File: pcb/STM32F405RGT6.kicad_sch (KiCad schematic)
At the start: 19 parts, among them U1 STM32F405RGTx, Y1 8MHz

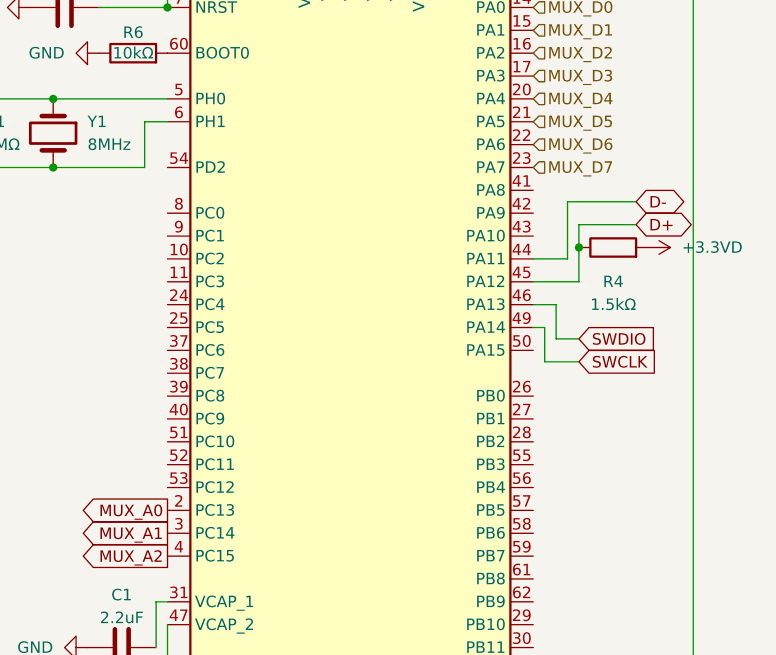
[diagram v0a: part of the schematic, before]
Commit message: feat: added the rotary encoder
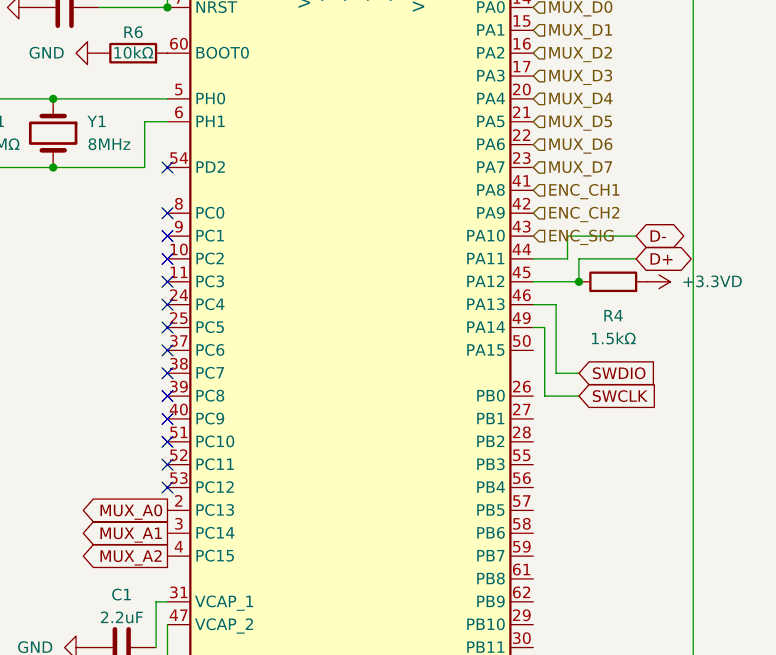
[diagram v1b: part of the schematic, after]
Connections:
- net ENC_CH1: now reaches U1.41 (PA8)
- net ENC_CH2: now reaches U1.42 (PA9)
- net ENC_SIG: now reaches U1.43 (PA10)
- no-connect marks 0 -> 14
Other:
- moved on the sheet: R4
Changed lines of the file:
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@@
+	)
+	(junction
+		(at 121.92 109.22)
+		(diameter 0)
+		(color 0 0 0 0)
 	)
 	(junction
@@
 	)
 	(junction
-		(at 121.92 105.41)
-		(diameter 0)
-		(color 0 0 0 0)
-	)
-	(junction
 		(at 53.34 88.9)
 		(diameter 0)
@@
 		(color 0 0 0 0)
 	)
-	(wire
-		(pts
-			(xy 121.92 102.87) (xy 128.27 102.87)
+	(no_connect
+		(at 76.2 132.08)
+	)
+	(no_connect
+		(at 76.2 114.3)
+	)
+	(no_connect
+		(at 76.2 101.6)
+	)
+	(no_connect
+		(at 76.2 104.14)
+	)
+	(no_connect
+		(at 76.2 129.54)
+	)
+	(no_connect
+		(at 76.2 127)
+	)
+	(no_connect
+		(at 76.2 106.68)
+	)
+	(no_connect
+		(at 76.2 121.92)
+	)
+	(no_connect
+		(at 76.2 111.76)
+	)
+	(no_connect
+		(at 76.2 109.22)
+	)
+	(no_connect
+		(at 76.2 124.46)
+	)
+	(no_connect
+		(at 76.2 119.38)
+	)
+	(no_connect
+		(at 76.2 96.52)
+	)
+	(no_connect
+		(at 76.2 116.84)
+	)
+	(wire
+		(pts
+			(xy 121.92 106.68) (xy 128.27 106.68)
 		)
 		(stroke
@@
 	(wire
 		(pts
-			(xy 120.65 100.33) (xy 128.27 100.33)
+			(xy 120.65 104.14) (xy 128.27 104.14)
 		)
 		(stroke
@@
 	(wire
 		(pts
-			(xy 121.92 102.87) (xy 121.92 105.41)
-		)
-		(stroke
-			(width 0)
-			(type default)
-		)
-	)
-	(wire
-		(pts
-			(xy 119.38 115.57) (xy 119.38 111.76)
+			(xy 119.38 119.38) (xy 119.38 111.76)
 		)
 		(stroke
@@
 	(wire
 		(pts
-			(xy 120.65 100.33) (xy 120.65 106.68)
+			(xy 120.65 104.14) (xy 120.65 106.68)
 		)
 		(stroke
@@
 	(wire
 		(pts
-			(xy 121.92 105.41) (xy 121.92 109.22)
-		)
-		(stroke
-			(width 0)
-			(type default)
-		)
-	)
-	(wire
-		(pts
 			(xy 125.73 45.72) (xy 125.73 46.99)
 		)
@@
 	(wire
 		(pts
-			(xy 121.92 118.11) (xy 118.11 118.11)
+			(xy 121.92 121.92) (xy 118.11 121.92)
 		)
 		(stroke
@@
 	(wire
 		(pts
-			(xy 118.11 118.11) (xy 118.11 114.3)
+			(xy 118.11 121.92) (xy 118.11 114.3)
+		)
+		(stroke
+			(width 0)
+			(type default)
+		)
+	)
+	(wire
+		(pts
+			(xy 121.92 106.68) (xy 121.92 109.22)
 		)
 		(stroke
@@
 	(wire
 		(pts
-			(xy 121.92 115.57) (xy 119.38 115.57)
+			(xy 121.92 119.38) (xy 119.38 119.38)
 		)
 		(stroke
@@
 	(global_label "D+"
 		(shape bidirectional)
-		(at 128.27 102.87 0)
+		(at 128.27 106.68 0)
 		(fields_autoplaced yes)
 		(effects
@@
 		)
 		(property "Intersheetrefs" "${INTERSHEET_REFS}"
-			(at 134.0976 102.87 0)
+			(at 134.0976 106.68 0)
 			(effects
 				(font
@@
 	(global_label "D-"
 		(shape bidirectional)
-		(at 128.27 100.33 0)
+		(at 128.27 104.14 0)
 		(fields_autoplaced yes)
 		(effects
@@
 		)
 		(property "Intersheetrefs" "${INTERSHEET_REFS}"
-			(at 134.0976 100.33 0)
+			(at 134.0976 104.14 0)
 			(effects
 				(font
@@
 	(global_label "SWCLK"
 		(shape input)
-		(at 121.92 118.11 0)
+		(at 121.92 121.92 0)
 		(fields_autoplaced yes)
 		(effects
@@
 		)
 		(property "Intersheetrefs" "${INTERSHEET_REFS}"
-			(at 131.1342 118.11 0)
+			(at 131.1342 121.92 0)
 			(effects
 				(font
@@
 	(global_label "SWDIO"
 		(shape input)
-		(at 121.92 115.57 0)
+		(at 121.92 119.38 0)
 		(fields_autoplaced yes)
 		(effects
@@
 		)
 		(property "Intersheetrefs" "${INTERSHEET_REFS}"
-			(at 130.7714 115.57 0)
+			(at 130.7714 119.38 0)
 			(effects
 				(font
@@
 		)
 	)
+	(hierarchical_label "ENC_SIG"
+		(shape input)
+		(at 116.84 104.14 0)
+		(effects
+			(font
+				(size 1.27 1.27)
+			)
+			(justify left)
+		)
+	)
 	(hierarchical_label "MUX_D1"
 		(shape input)
 		(at 116.84 81.28 0)
+		(effects
+			(font
+				(size 1.27 1.27)
+			)
+			(justify left)
+		)
+	)
+	(hierarchical_label "ENC_CH2"
+		(shape input)
+		(at 116.84 101.6 0)
+		(effects
+			(font
+				(size 1.27 1.27)
+			)
+			(justify left)
+		)
+	)
+	(hierarchical_label "ENC_CH1"
+		(shape input)
+		(at 116.84 99.06 0)
 		(effects
 			(font
@@
 	(symbol
 		(lib_id "Device:R")
-		(at 125.73 105.41 90)
+		(at 125.73 109.22 90)
 		(unit 1)
 		(exclude_from_sim no)
@@
 		(fields_autoplaced yes)
 		(property "Reference" "R4"
-			(at 125.73 109.22 90)
+			(at 125.73 113.03 90)
 			(effects
 				(font
@@
 		)
 		(property "Value" "1.5kΩ"
-			(at 125.73 111.76 90)
+			(at 125.73 115.57 90)
 			(effects
 				(font
@@
 		)
 		(property "Footprint" ""
-			(at 125.73 107.188 90)
+			(at 125.73 110.998 90)
 			(effects
 				(font
@@
 		)
 		(property "Datasheet" "~"
-			(at 125.73 105.41 0)
+			(at 125.73 109.22 0)
 			(effects
 				(font
@@
 		)
 		(property "Description" "Resistor"
-			(at 125.73 105.41 0)
+			(at 125.73 109.22 0)
 			(effects
 				(font
@@
 	(symbol
 		(lib_id "power:+3.3V")
-		(at 129.54 105.41 270)
+		(at 129.54 109.22 270)
 		(unit 1)
 		(exclude_from_sim no)
@@
 		(fields_autoplaced yes)
 		(property "Reference" "#PWR027"
-			(at 125.73 105.41 0)
+			(at 125.73 109.22 0)
 			(effects
 				(font
@@
 		)
 		(property "Value" "+3.3VD"
-			(at 133.35 105.4099 90)
+			(at 133.35 109.2199 90)
 			(effects
 				(font
@@
 		)
 		(property "Footprint" ""
-			(at 129.54 105.41 0)
+			(at 129.54 109.22 0)
 			(effects
 				(font
@@
 		)
 		(property "Datasheet" ""
-			(at 129.54 105.41 0)
+			(at 129.54 109.22 0)
 			(effects
 				(font
@@
 		)
 		(property "Description" "Power symbol creates a global label with name \"+3.3V\""
-			(at 129.54 105.41 0)
-			(effects
-				(font
+			(at 129.54 109.22 0)
+			(effects
+				(font

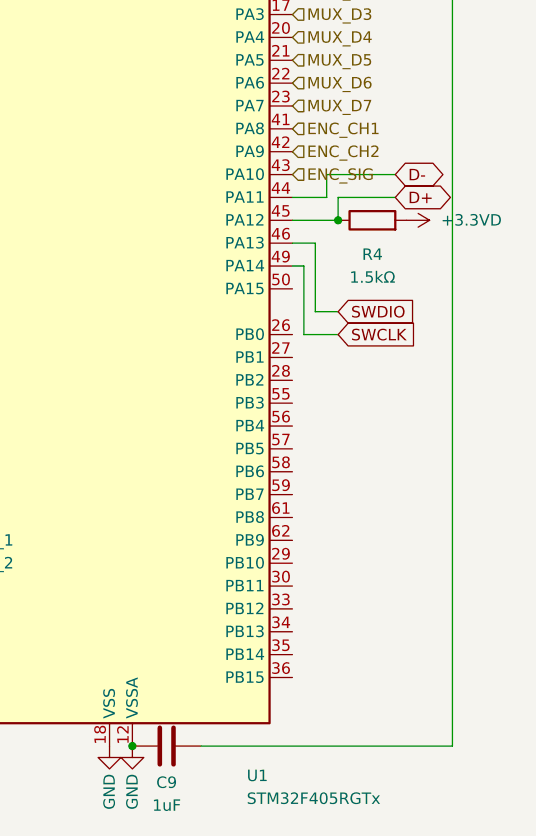
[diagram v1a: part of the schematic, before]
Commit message: fix: moved D- and D+ to PB14 and PB15 for USB High Speed rather
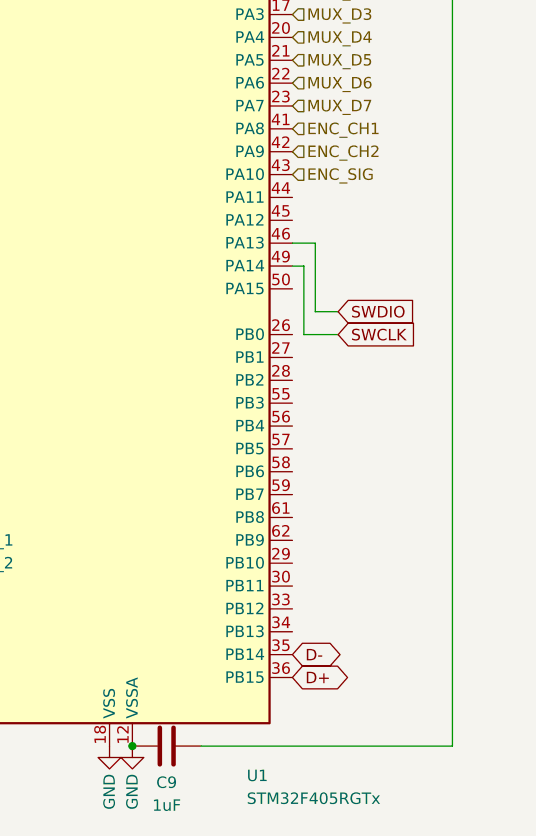
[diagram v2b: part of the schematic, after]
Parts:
- removed R4: 1.5kΩ, symbol Device:R
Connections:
- net D+: now also U1.36 (PB15); no longer U1.45 (PA12)
- net D-: now also U1.35 (PB14); no longer U1.44 (PA11)
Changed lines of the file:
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@@
-	)
-	(junction
-		(at 121.92 109.22)
-		(diameter 0)
-		(color 0 0 0 0)
 	)
 	(junction
@@
 	(wire
 		(pts
-			(xy 121.92 106.68) (xy 128.27 106.68)
-		)
-		(stroke
-			(width 0)
-			(type default)
-		)
-	)
-	(wire
-		(pts
 			(xy 104.14 71.12) (xy 104.14 50.8)
 		)
@@
 	(wire
 		(pts
-			(xy 120.65 106.68) (xy 116.84 106.68)
-		)
-		(stroke
-			(width 0)
-			(type default)
-		)
-	)
-	(wire
-		(pts
 			(xy 71.12 46.99) (xy 74.93 46.99)
 		)
@@
 	(wire
 		(pts
-			(xy 120.65 104.14) (xy 128.27 104.14)
-		)
-		(stroke
-			(width 0)
-			(type default)
-		)
-	)
-	(wire
-		(pts
 			(xy 134.62 50.8) (xy 134.62 167.64)
 		)
@@
 	(wire
 		(pts
-			(xy 120.65 104.14) (xy 120.65 106.68)
-		)
-		(stroke
-			(width 0)
-			(type default)
-		)
-	)
-	(wire
-		(pts
 			(xy 76.2 91.44) (xy 73.66 91.44)
 		)
@@
 	(wire
 		(pts
-			(xy 121.92 109.22) (xy 116.84 109.22)
-		)
-		(stroke
-			(width 0)
-			(type default)
-		)
-	)
-	(wire
-		(pts
 			(xy 53.34 88.9) (xy 63.5 88.9)
 		)
@@
 		(pts
 			(xy 118.11 121.92) (xy 118.11 114.3)
-		)
-		(stroke
-			(width 0)
-			(type default)
-		)
-	)
-	(wire
-		(pts
-			(xy 121.92 106.68) (xy 121.92 109.22)
 		)
 		(stroke
@@
 	(global_label "D+"
 		(shape bidirectional)
-		(at 128.27 106.68 0)
+		(at 116.84 160.02 0)
 		(fields_autoplaced yes)
 		(effects
@@
 		)
 		(property "Intersheetrefs" "${INTERSHEET_REFS}"
-			(at 134.0976 106.68 0)
+			(at 122.6676 160.02 0)
 			(effects
 				(font
@@
 		)
 	)
-	(global_label "D-"
-		(shape bidirectional)
-		(at 128.27 104.14 0)
-		(fields_autoplaced yes)
-		(effects
-			(font
-				(size 1.27 1.27)
-			)
-			(justify left)
-		)
-		(property "Intersheetrefs" "${INTERSHEET_REFS}"
-			(at 134.0976 104.14 0)
-			(effects
-				(font
-					(size 1.27 1.27)
-				)
-				(justify left)
-				(hide yes)
-			)
-		)
-	)
 	(global_label "SWCLK"
 		(shape input)
@@
 				)
 				(justify right)
+				(hide yes)
+			)
+		)
+	)
+	(global_label "D-"
+		(shape bidirectional)
+		(at 116.84 157.48 0)
+		(fields_autoplaced yes)
+		(effects
+			(font
+				(size 1.27 1.27)
+			)
+			(justify left)
+		)
+		(property "Intersheetrefs" "${INTERSHEET_REFS}"
+			(at 122.6676 157.48 0)
+			(effects
+				(font
+					(size 1.27 1.27)
+				)
+				(justify left)
 				(hide yes)
 			)
@@
 					(unit 1)
 				)
-			)
-		)
-	)
-	(symbol
-		(lib_id "Device:R")
-		(at 125.73 109.22 90)
-		(unit 1)
-		(exclude_from_sim no)
-		(in_bom yes)
-		(on_board yes)
-		(dnp no)
-		(fields_autoplaced yes)
-		(property "Reference" "R4"
-			(at 125.73 113.03 90)
-			(effects
-				(font
-					(size 1.27 1.27)
-				)
-			)
-		)
-		(property "Value" "1.5kΩ"
-			(at 125.73 115.57 90)
-			(effects
-				(font
-					(size 1.27 1.27)
-				)
-			)
-		)
-		(property "Footprint" ""
-			(at 125.73 110.998 90)
-			(effects
-				(font
-					(size 1.27 1.27)
-				)
-				(hide yes)
-			)
-		)
-		(property "Datasheet" "~"
-			(at 125.73 109.22 0)
-			(effects
-				(font
-					(size 1.27 1.27)
-				)
-				(hide yes)
-			)
-		)
-		(property "Description" "Resistor"
-			(at 125.73 109.22 0)
-			(effects
-				(font
-					(size 1.27 1.27)
-				)
-				(hide yes)
-			)
-		)
-		(pin "1"
-		)
-		(pin "2"
-		)
-		(instances
-			(project "prometheus-65"
-				(path "/7080535f-072d-4fc6-b033-a9cfe8594544/86ea6946-9a6c-47e9-ad6e-248d3f456e58"
-					(reference "R4")
-					(unit 1)
-				)
-			)
-		)
-	)
-	(symbol
-		(lib_id "power:+3.3V")
-		(at 129.54 109.22 270)
-		(unit 1)
-		(exclude_from_sim no)
-		(in_bom yes)
-		(on_board yes)
-		(dnp no)
-		(fields_autoplaced yes)
-		(property "Reference" "#PWR027"
-			(at 125.73 109.22 0)
-			(effects
-				(font
-					(size 1.27 1.27)
-				)
-				(hide yes)
-			)
-		)
-		(property "Value" "+3.3VD"
-			(at 133.35 109.2199 90)
-			(effects
-				(font
-					(size 1.27 1.27)
-				)
-				(justify left)
-			)
-		)
-		(property "Footprint" ""
-			(at 129.54 109.22 0)
-			(effects
-				(font
-					(size 1.27 1.27)
-				)
-				(hide yes)
-			)
-		)
-		(property "Datasheet" ""
-			(at 129.54 109.22 0)
-			(effects
-				(font
-					(size 1.27 1.27)
-				)
-				(hide yes)
-			)
-		)
-		(property "Description" "Power symbol creates a global label with name \"+3.3V\""
-			(at 129.54 109.22 0)
-			(effects
-				(font
-					(size 1.27 1.27)
-				)
-				(hide yes)
-			)
-		)
-		(pin "1"
-		)
-		(instances
-			(project "prometheus-65"
-				(path "/7080535f-072d-4fc6-b033-a9cfe8594544/86ea6946-9a6c-47e9-ad6e-248d3f456e58"
-					(reference "#PWR027")
-					(unit 1)
-				)

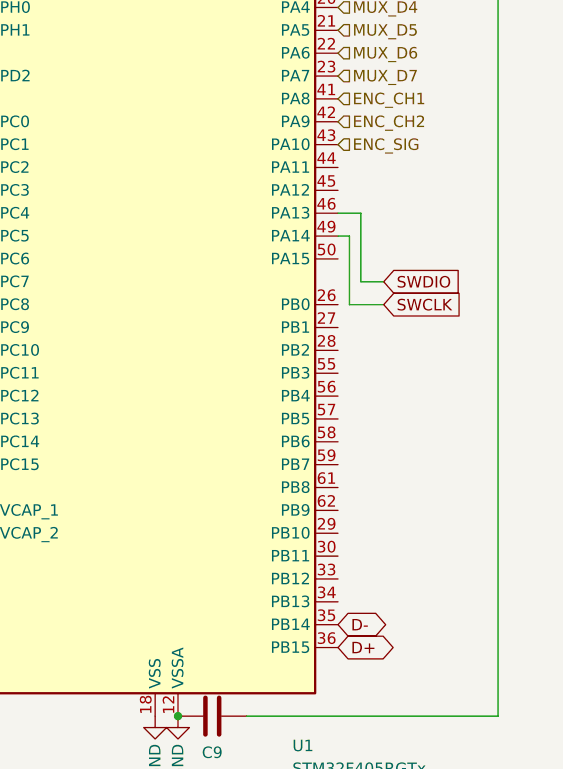
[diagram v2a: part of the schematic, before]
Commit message: feat: added LED circuit and wired to STM32
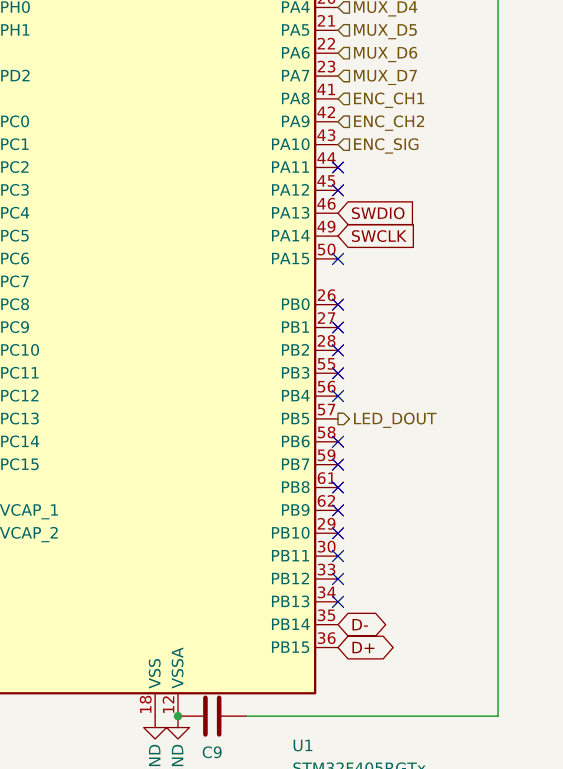
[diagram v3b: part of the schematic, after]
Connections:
- net LED_DOUT: now reaches U1.57 (PB5)
- no-connect marks 14 -> 30
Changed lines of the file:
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@@
+	)
+	(no_connect
+		(at 116.84 142.24)
+	)
+	(no_connect
+		(at 116.84 129.54)
 	)
 	(no_connect
@@
 	)
 	(no_connect
+		(at 116.84 106.68)
+	)
+	(no_connect
+		(at 116.84 127)
+	)
+	(no_connect
+		(at 116.84 132.08)
+	)
+	(no_connect
 		(at 76.2 101.6)
 	)
 	(no_connect
+		(at 116.84 121.92)
+	)
+	(no_connect
+		(at 116.84 139.7)
+	)
+	(no_connect
+		(at 116.84 109.22)
+	)
+	(no_connect
+		(at 116.84 149.86)
+	)
+	(no_connect
 		(at 76.2 104.14)
 	)
@@
 	)
 	(no_connect
+		(at 116.84 152.4)
+	)
+	(no_connect
 		(at 76.2 127)
 	)
@@
 	)
 	(no_connect
+		(at 116.84 124.46)
+	)
+	(no_connect
 		(at 76.2 109.22)
 	)
 	(no_connect
+		(at 116.84 137.16)
+	)
+	(no_connect
 		(at 76.2 124.46)
 	)
 	(no_connect
+		(at 116.84 116.84)
+	)
+	(no_connect
 		(at 76.2 119.38)
 	)
@@
 	)
 	(no_connect
+		(at 116.84 144.78)
+	)
+	(no_connect
+		(at 116.84 154.94)
+	)
+	(no_connect
+		(at 116.84 147.32)
+	)
+	(no_connect
 		(at 76.2 116.84)
 	)
@@
 	(wire
 		(pts
-			(xy 118.11 114.3) (xy 116.84 114.3)
-		)
-		(stroke
-			(width 0)
-			(type default)
-		)
-	)
-	(wire
-		(pts
 			(xy 71.12 43.18) (xy 71.12 46.99)
 		)
@@
 	(wire
 		(pts
-			(xy 119.38 119.38) (xy 119.38 111.76)
-		)
-		(stroke
-			(width 0)
-			(type default)
-		)
-	)
-	(wire
-		(pts
 			(xy 48.26 96.52) (xy 53.34 96.52)
 		)
@@
 	(wire
 		(pts
-			(xy 119.38 111.76) (xy 116.84 111.76)
-		)
-		(stroke
-			(width 0)
-			(type default)
-		)
-	)
-	(wire
-		(pts
 			(xy 74.93 156.21) (xy 76.2 156.21)
 		)
@@
 	(wire
 		(pts
-			(xy 121.92 121.92) (xy 118.11 121.92)
-		)
-		(stroke
-			(width 0)
-			(type default)
-		)
-	)
-	(wire
-		(pts
 			(xy 99.06 71.12) (xy 99.06 48.26)
 		)
@@
 	(wire
 		(pts
-			(xy 118.11 121.92) (xy 118.11 114.3)
-		)
-		(stroke
-			(width 0)
-			(type default)
-		)
-	)
-	(wire
-		(pts
 			(xy 101.6 49.53) (xy 101.6 71.12)
 		)
@@
 		(pts
 			(xy 74.93 161.29) (xy 74.93 156.21)
-		)
-		(stroke
-			(width 0)
-			(type default)
-		)
-	)
-	(wire
-		(pts
-			(xy 121.92 119.38) (xy 119.38 119.38)
 		)
 		(stroke
@@
 	(global_label "SWCLK"
 		(shape input)
-		(at 121.92 121.92 0)
+		(at 116.84 114.3 0)
 		(fields_autoplaced yes)
 		(effects
@@
 		)
 		(property "Intersheetrefs" "${INTERSHEET_REFS}"
-			(at 131.1342 121.92 0)
+			(at 126.0542 114.3 0)
 			(effects
 				(font
@@
 	(global_label "SWDIO"
 		(shape input)
-		(at 121.92 119.38 0)
+		(at 116.84 111.76 0)
 		(fields_autoplaced yes)
 		(effects
@@
 		)
 		(property "Intersheetrefs" "${INTERSHEET_REFS}"
-			(at 130.7714 119.38 0)
+			(at 125.6914 111.76 0)
 			(effects
 				(font
@@
 		(effects
 			(font
+				(size 1.27 1.27)
+			)
+			(justify left)
+		)
+	)
+	(hierarchical_label "LED_DOUT"
+		(shape output)
+		(at 116.84 134.62 0)
+		(effects
+			(font
